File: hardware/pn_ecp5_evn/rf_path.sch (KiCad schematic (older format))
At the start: 39 parts, among them J701 Conn_Coaxial, J702 Conn_Coaxial, J703 Conn_Coaxial, U701 SYM-63LH+, U702 ADG621, U703 OPA2211

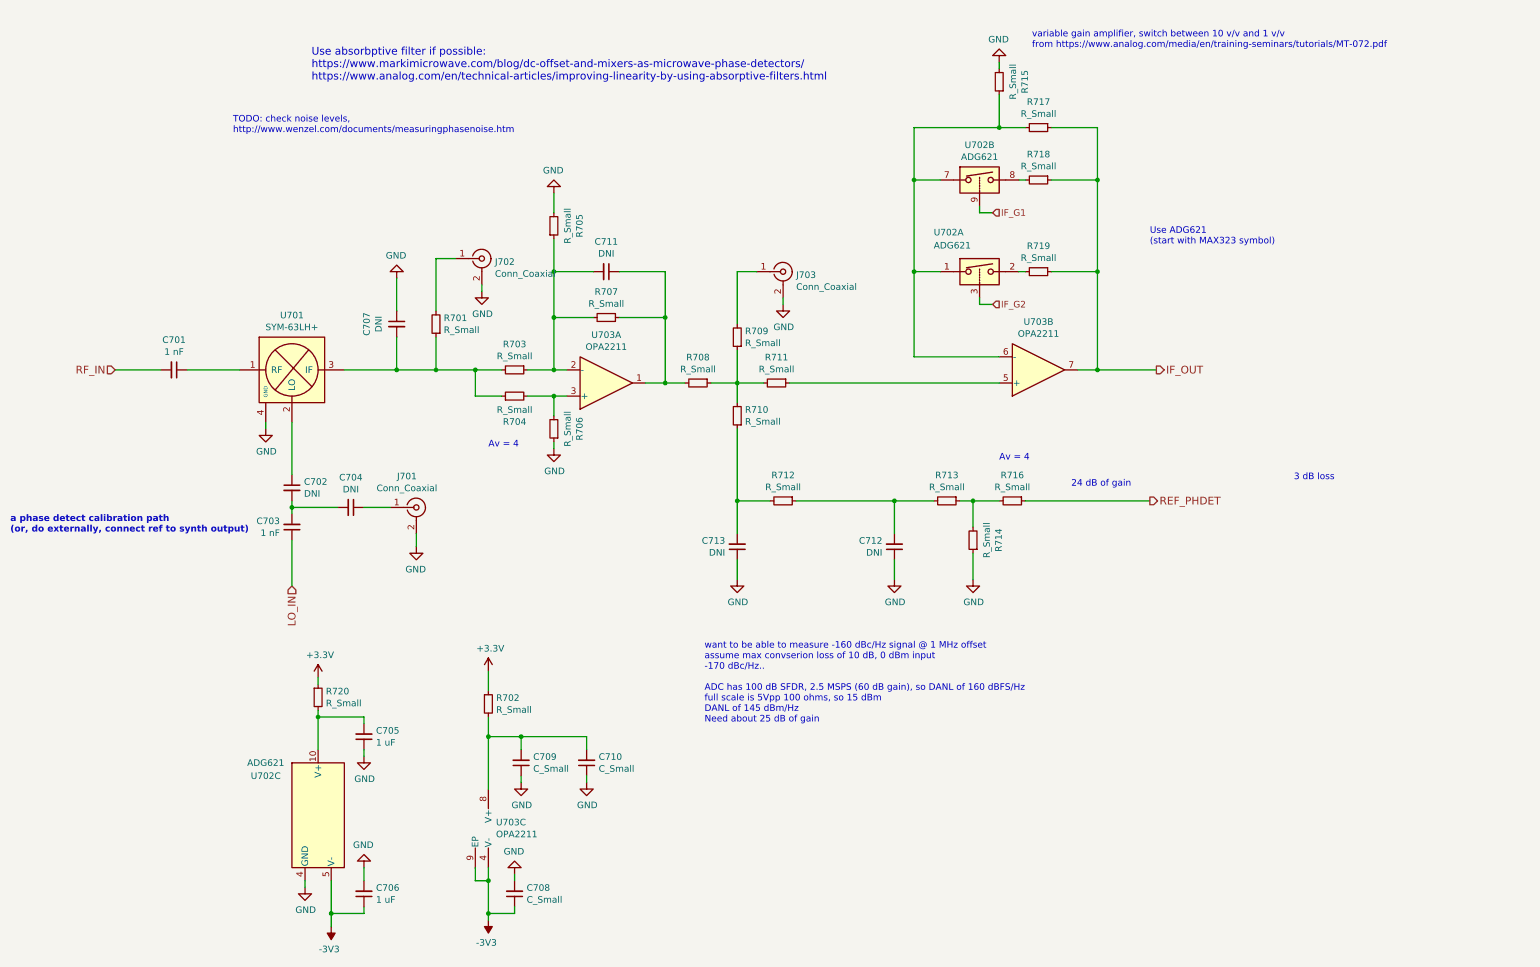
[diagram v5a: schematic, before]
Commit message: checked stability of LO amplifier, started migen project, added more flexibility for active filtering on baseband path
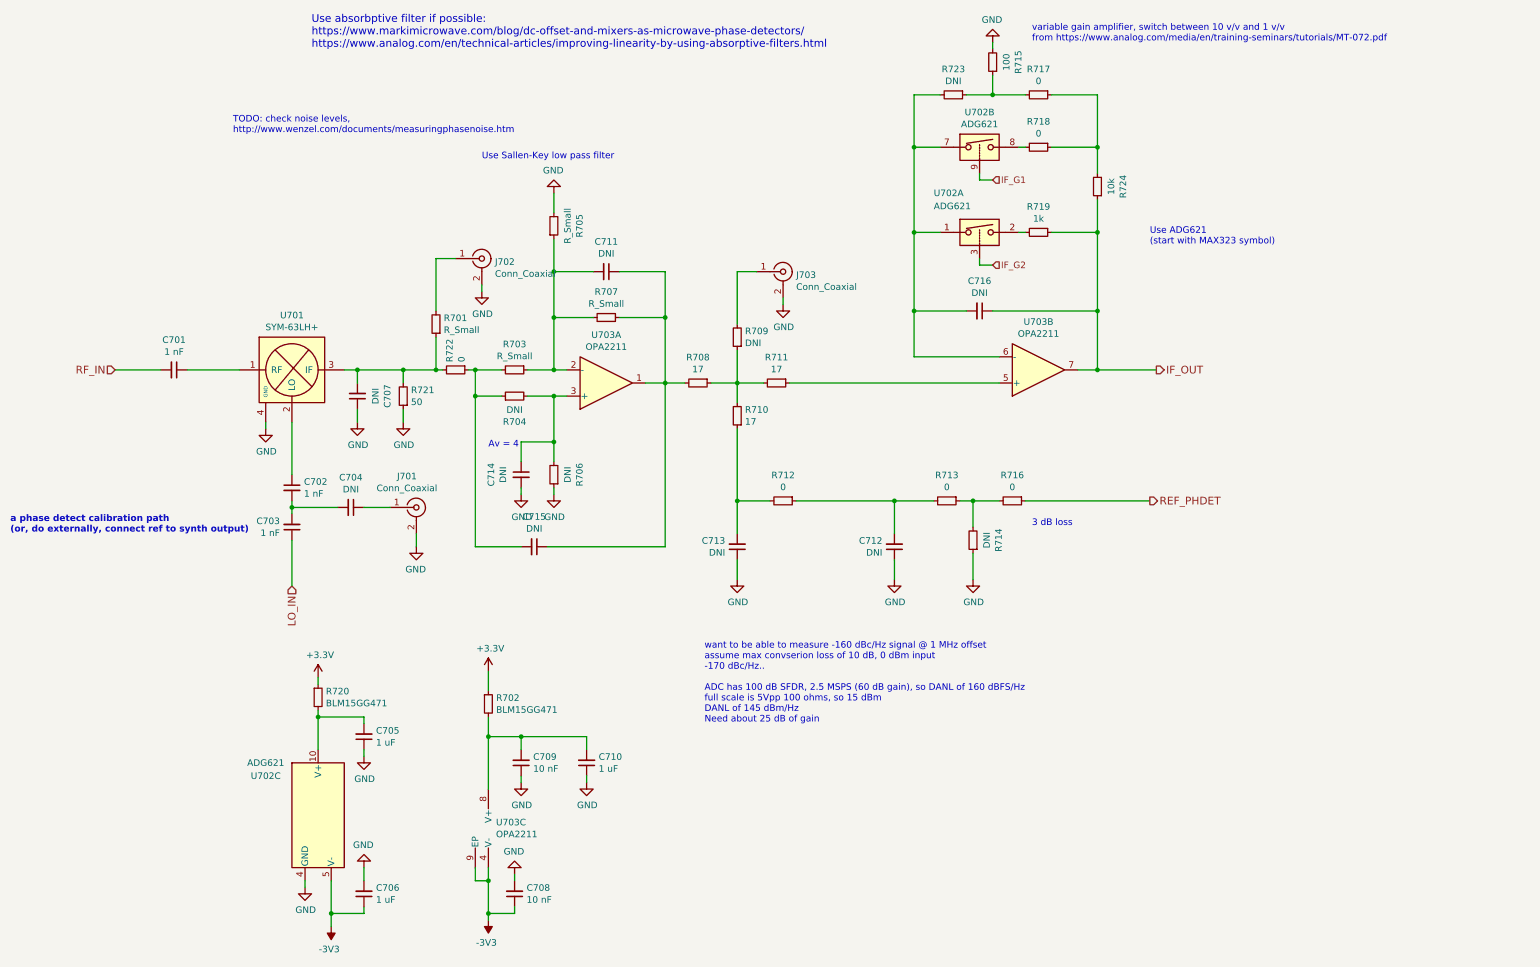
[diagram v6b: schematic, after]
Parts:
- added C714, C715, C716: DNI, Capacitor_SMD:C_0603_1608Metric, symbol Device:C_Small
- added R721: 50, Resistor_SMD:R_0402_1005Metric, symbol Device:R_Small
- added R722: 0, Resistor_SMD:R_0402_1005Metric, symbol Device:R_Small
- added R723: DNI, Resistor_SMD:R_0402_1005Metric, symbol Device:R_Small
- added R724: 10k, Resistor_SMD:R_0402_1005Metric, symbol Device:R_Small
- C702: value DNI -> 1 nF
- C708, C709: value C_Small -> 10 nF
- C710: value C_Small -> 1 uF
- C711: footprint Capacitor_SMD:C_0402_1005Metric -> Capacitor_SMD:C_0603_1608Metric
- R702, R720: value R_Small -> BLM15GG471
- R704, R706, R709, R714: value R_Small -> DNI
- R708, R710, R711: value R_Small -> 17
- R712, R713, R716, R717, R718: value R_Small -> 0
- R715: value R_Small -> 100
- R719: value R_Small -> 1k
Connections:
- net GND: now also C714.2, R721.1
- net IF_OUT: now also C716.1, R724.1; no longer R717.1, R718.1
- net at C707.2, R701.1, U701.3 (IF): now also R721.2, R722.2; no longer R703.2, R704.1
- net at C711.1, R707.1, R708.2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: now also C715.1
- net at R704.2, R706.2, U703.3 (+): now also C714.1
- net at U702.1, U702.7, U703.6 (-): now also C716.2, R723.2; no longer R715.1, R717.2
- new net: C715.2, R703.2, R704.1, R722.1
- new net: R717.1, R718.1, R724.2
- new net: R715.1, R717.2, R723.1
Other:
- note added: "Use Sallen-Key low pass filter"
- note removed: "24 dB of gain"
- moved on the sheet: C707, R706, R715, R717, R718, R719, U702A, U702B

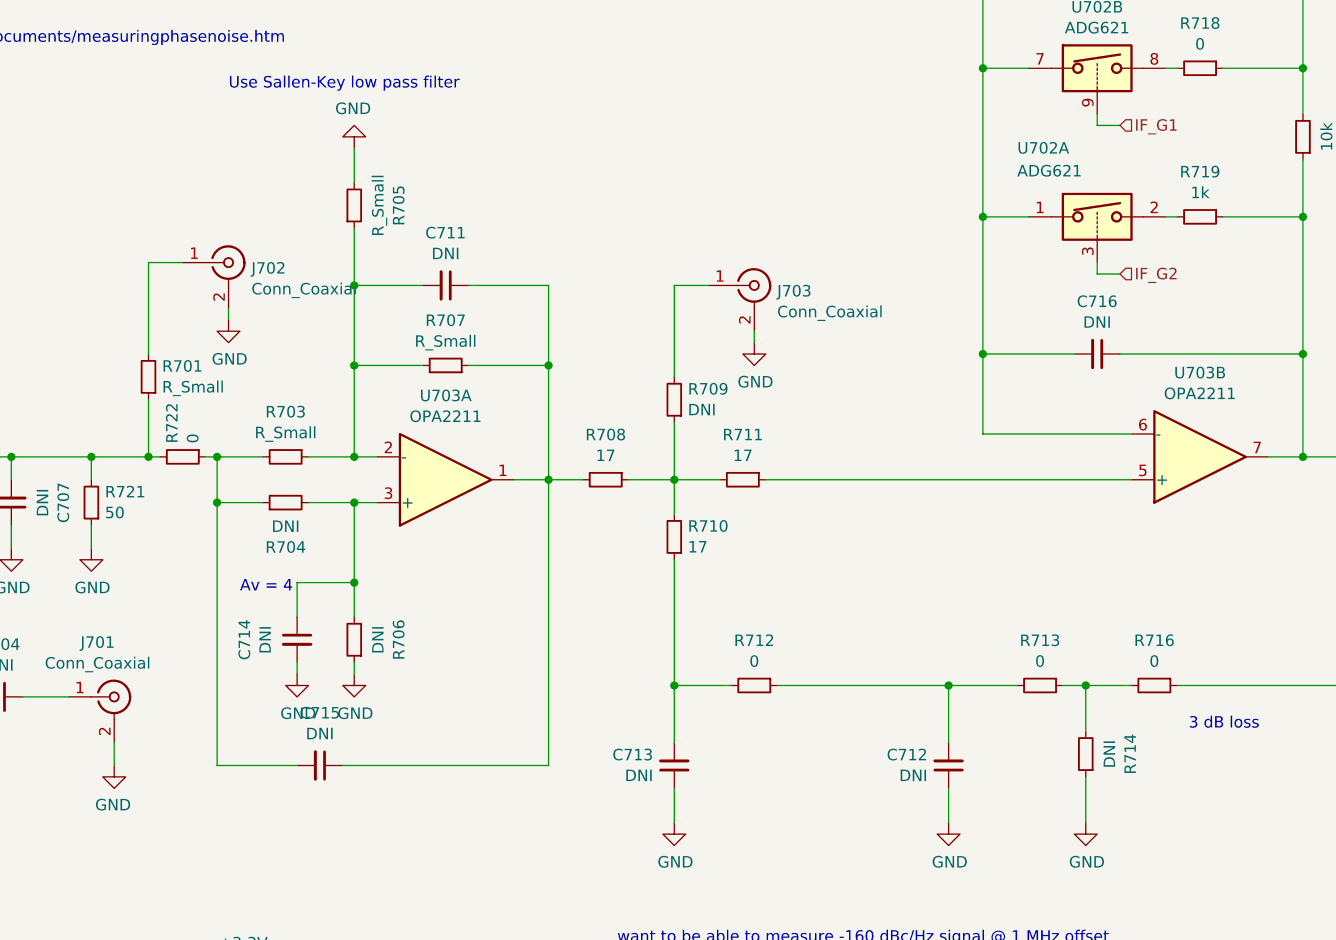
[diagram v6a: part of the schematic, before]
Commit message: added part numbers to schematic of phase noise downconverter, ordered
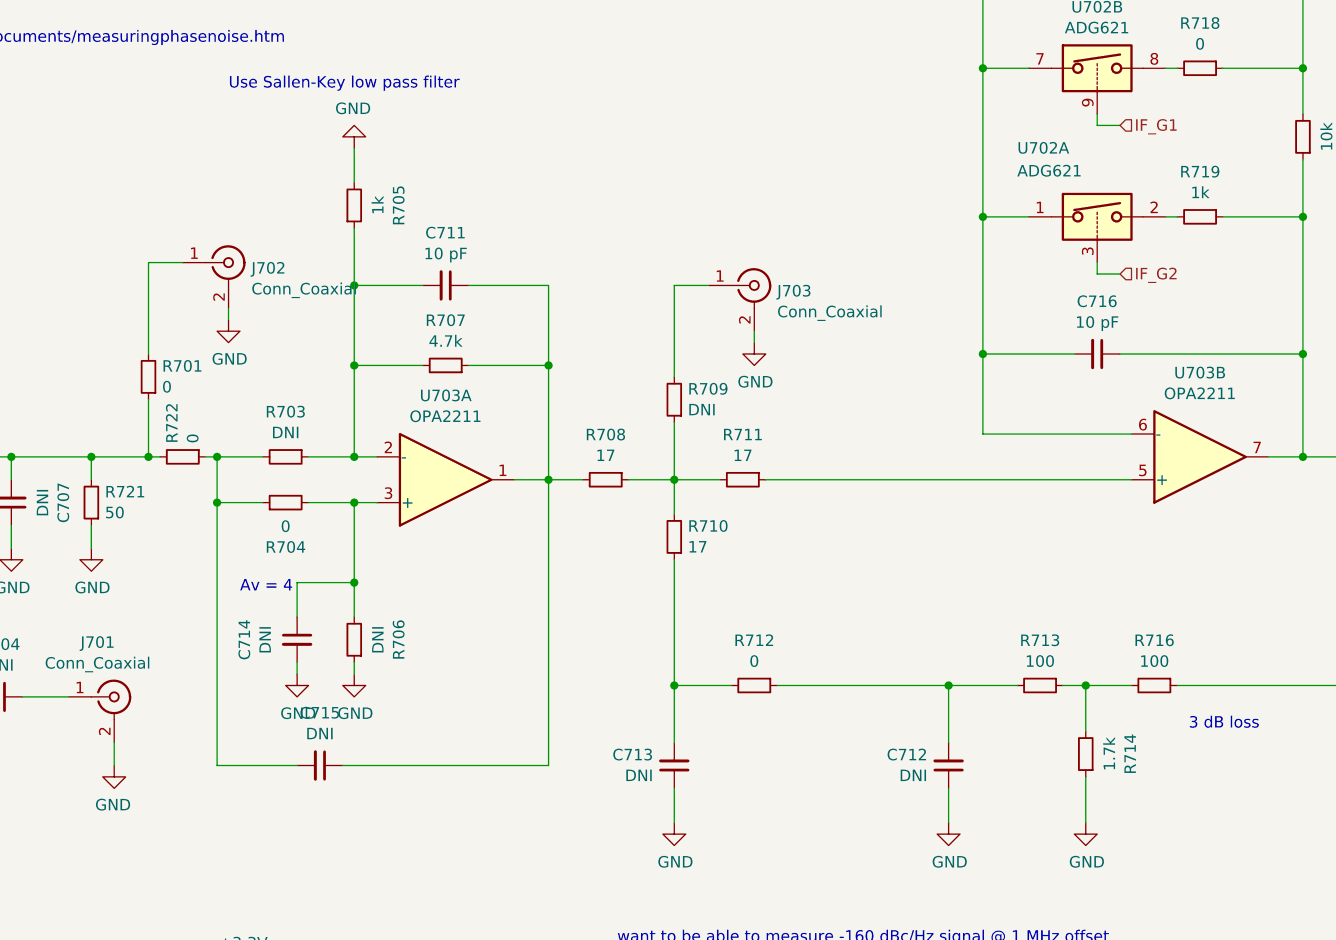
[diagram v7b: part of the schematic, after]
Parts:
- C701, C702, C703, C704, C705, C706, C707, C708, C709, C710, C712, C713, C714, C715, J701, J702, J703, R706, R708, R709, R710, R711, R723, R724: Distributor Part Number (none) -> N/A
- C711, C716: value DNI -> 10 pF; Distributor (none) -> Digi-Key; Distributor Part Number (none) -> 311-1058-1-ND
- R701: value R_Small -> 0; Distributor (none) -> Digi-Key; Distributor Part Number (none) -> P0.0JCT-ND
- R702, R720: Distributor (none) -> Digi-Key; Distributor Part Number (none) -> 490-5198-1-ND
- R703: value R_Small -> DNI; Distributor Part Number (none) -> N/A
- R704: value DNI -> 0; Distributor (none) -> Digi-Key; Distributor Part Number (none) -> P0.0JCT-ND
- R705: value R_Small -> 1k; Distributor (none) -> Digi-Key; Distributor Part Number (none) -> RR05P1.0KDCT-ND
- R707: value R_Small -> 4.7k; Distributor Part Number (none) -> N/A
- R712, R717, R718, R722: Distributor (none) -> Digi-Key; Distributor Part Number (none) -> P0.0JCT-ND
- R713, R716: value 0 -> 100; Distributor (none) -> Digi-Key; Distributor Part Number (none) -> RR05P100DCT-ND
- R714: value DNI -> 1.7k; Distributor Part Number (none) -> N/A
- R715: Distributor (none) -> Digi-Key; Distributor Part Number (none) -> RR05P100DCT-ND
- R719: Distributor (none) -> Digi-Key; Distributor Part Number (none) -> RR05P1.0KDCT-ND
- R721: Distributor (none) -> Digi-Key; Distributor Part Number (none) -> RR05R49.9DCT-ND
- U701: Distributor (none) -> Mouser; Distributor Part Number (none) -> 139-SYM-63LH
- U702: Distributor (none) -> Digi-Key; Distributor Part Number (none) -> ADG621BRMZ-REELCT-ND
- U703: Distributor (none) -> Digi-Key; Distributor Part Number (none) -> 296-43607-1-ND

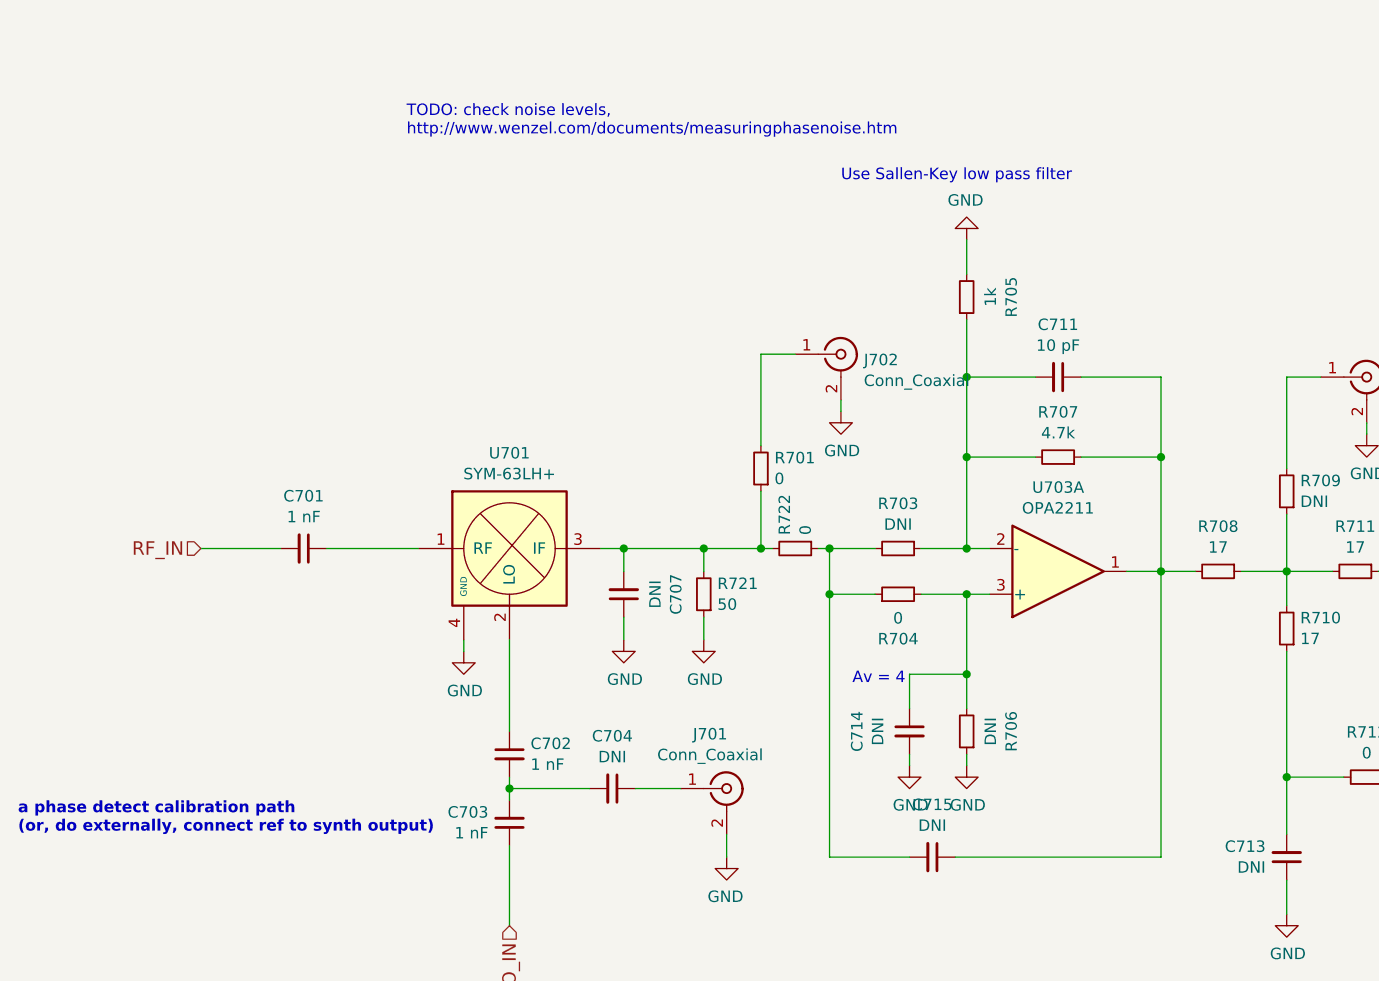
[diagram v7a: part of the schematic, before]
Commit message: added schematic export, updated README, schematic cleanup
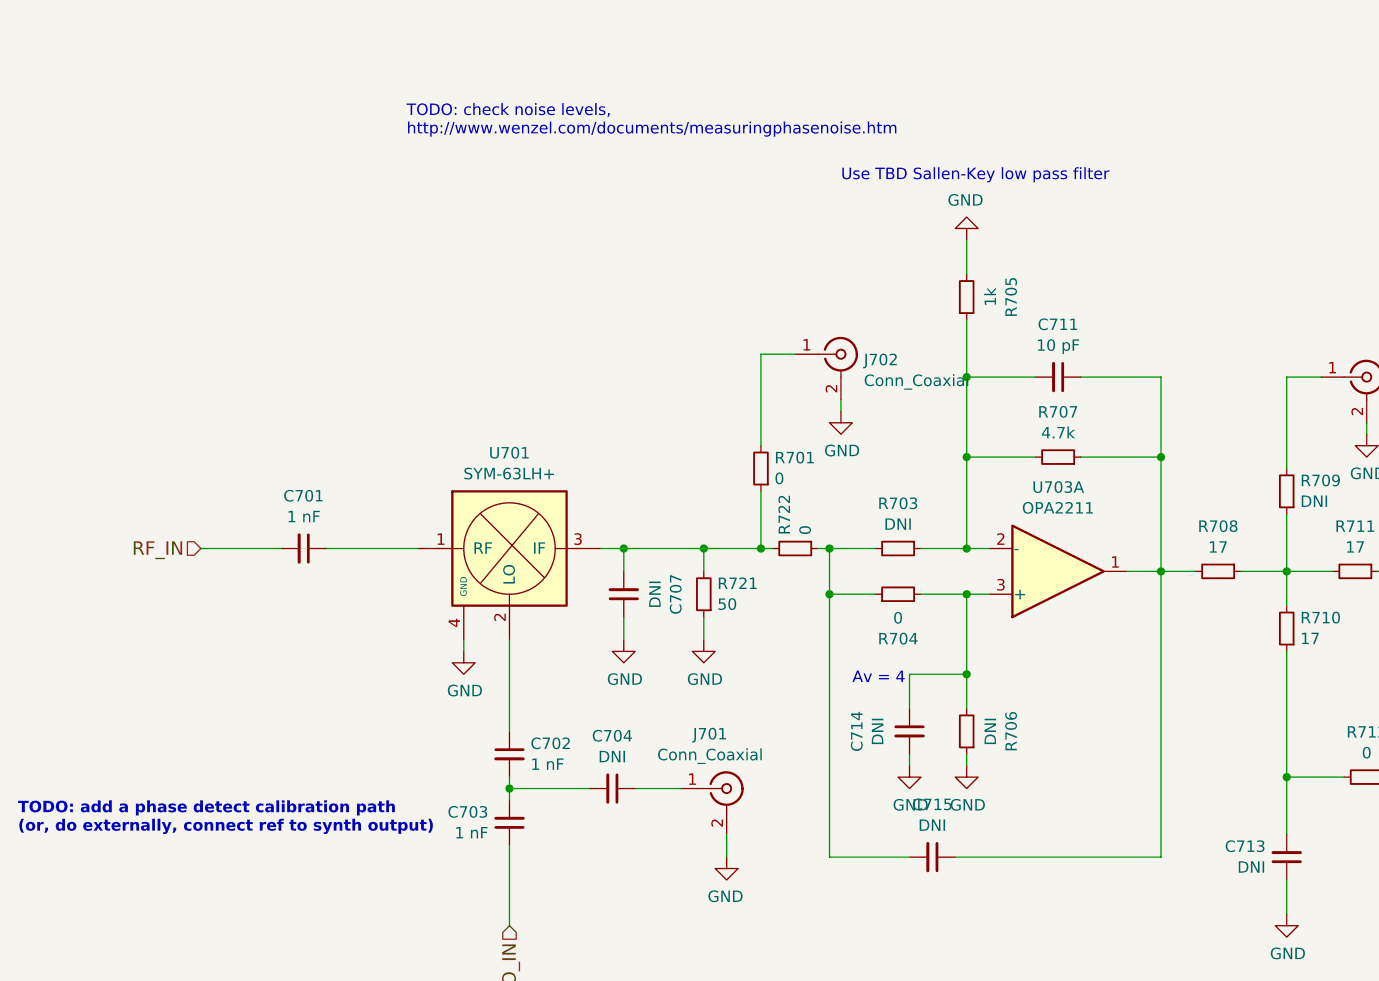
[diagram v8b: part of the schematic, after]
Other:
- note added: "TODO: add a phase detect calibration path\n(or, do externally, connect ref to synth output)"
- note added: "Use TBD Sallen-Key low pass filter"
- note removed: "Use Sallen-Key low pass filter"
- note removed: "a phase detect calibration path\n(or, do externally, connect ref to synth output)"
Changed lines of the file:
@@
 $EndComp
 Text Notes 600  4450 0    50   ~ 10
-a phase detect calibration path\n(or, do externally, connect ref to synth output)
+TODO: add a phase detect calibration path\n(or, do externally, connect ref to synth output)
 $Comp
 L Device:C_Small C703
@@
 	3250 3300 3250 3200
 Text Notes 4200 1600 0    50   ~ 0
-Use Sallen-Key low pass filter
+Use TBD Sallen-Key low pass filter
 $Comp
 L Device:C_Small C715
